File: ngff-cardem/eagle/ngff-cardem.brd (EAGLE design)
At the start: 90 x 100 mm, 150 parts, among them IC201 CB3Q3244PW, IC202 CB3Q3244PW, IC203 IP4234CZ6, IC204 FPF2109, IC205 FPF2109, IC301 TPS22958N-DGN, IC302 TPS22958N-DGK, J301 PJ-002BH-SMT-TR, M2 MENTOR_12701001, M3 MENTOR_12701001, Q201 12MHz, T101 BC850, T102 BC850, U201 IP4234CZ6, U202 AT91SAM3S-AU, U301 MIC5366-1.8YC5, X101 PINHD-2X3-SP, X102 ZX360D-B-10P(30), X201 MINI-USB-SHIELD-UX60-MB-5ST, X202 2.54mm, X203 JACK2.5_SJ-2523, X301 171826-4-RA

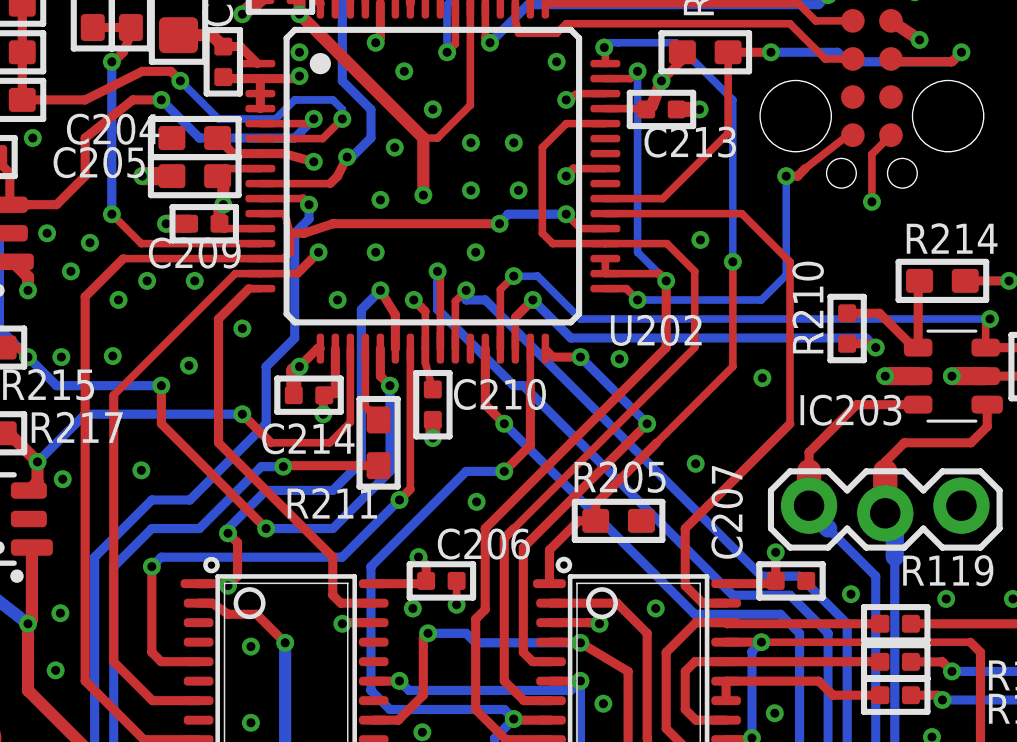
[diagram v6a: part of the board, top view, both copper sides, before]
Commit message: ngff-cardem: insert 2 PUs as DNP for possible !CONNECT_UART{1,2} biasing
solves SYS#5532
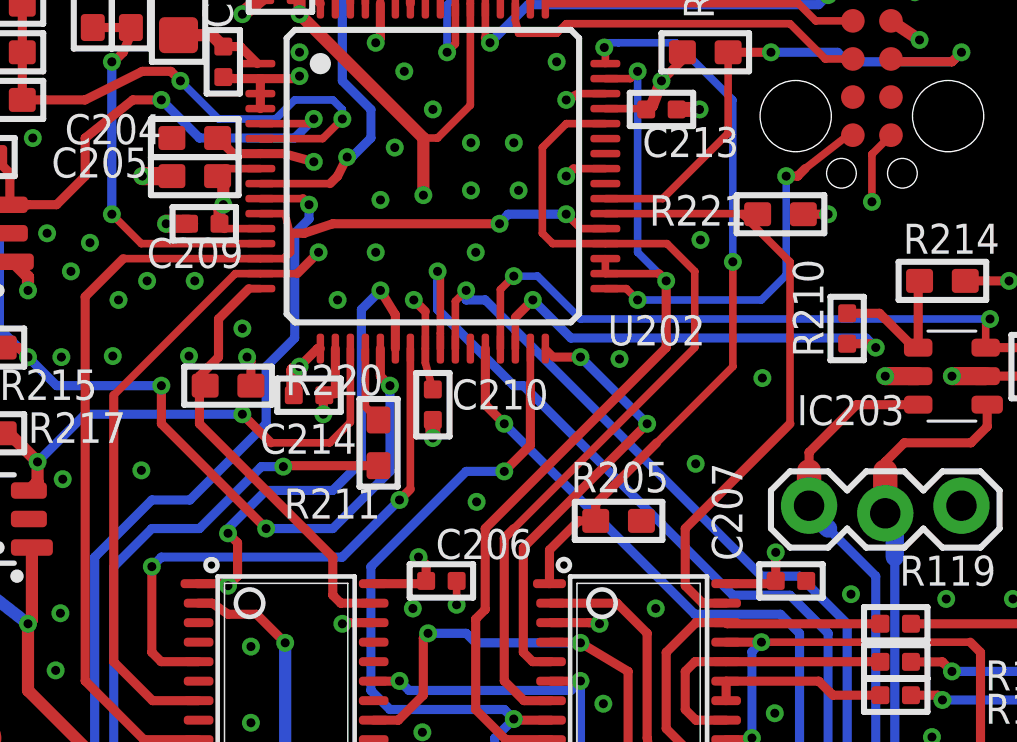
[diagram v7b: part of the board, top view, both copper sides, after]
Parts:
- added R220, R221: DNP, rc-sysmocom:_0603
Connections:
- net !CONNECT_UART1: now also R220.2
- net !CONNECT_UART2: now also R221.2
- net VCC_3V3: now also R220.1, R221.1
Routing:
- net VCC_3V3: track 56.6 -> 58.5 mm, vias 26 -> 28
- net !CONNECT_UART1: track 14.1 -> 14.8 mm
- net !CONNECT_UART2: track 20.7 -> 21.2 mm
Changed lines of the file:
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@@
 <attribute name="NAME" x="88.4875" y="77.31" size="1.1" layer="25" ratio="15" rot="R180"/>
 <attribute name="VALUE" x="89.3775" y="90.5825" size="1.27" layer="27" rot="R180"/>
-<attribute name="DESCRIPTION" value="" x="84.9325" y="83.5975" size="1.778" layer="27" rot="R180" display="off"/>
-<attribute name="MANUFACTURER" value="" x="84.9325" y="83.5975" size="1.778" layer="27" rot="R180" display="off"/>
-<attribute name="MANUFACTURERPARTNUMBER" value="" x="84.9325" y="83.5975" size="1.778" layer="27" rot="R180" display="off"/>
+<attribute name="DESCRIPTION" value="NO DESCRIPTION" x="84.9325" y="83.5975" size="1.778" layer="27" rot="R180" display="off"/>
+<attribute name="MANUFACTURER" value="UNKNOWN MANUFACTURER" x="84.9325" y="83.5975" size="1.778" layer="27" rot="R180" display="off"/>
+<attribute name="MANUFACTURERPARTNUMBER" value="UNKNOWN MANUFACTURER PART NUMBER" x="84.9325" y="83.5975" size="1.778" layer="27" rot="R180" display="off"/>
 <attribute name="SOURCE" value="DIGIKEY" x="84.9325" y="83.5975" size="1.778" layer="27" rot="R180" display="off"/>
-<attribute name="SOURCEPARTNUMBER" value="" x="84.9325" y="83.5975" size="1.778" layer="27" rot="R180" display="off"/>
-<attribute name="ROHSCERTIFICATE" value="" x="84.9325" y="83.5975" size="1.778" layer="27" rot="R180" display="off"/>
+<attribute name="SOURCEPARTNUMBER" value="UNKNOWN SOURCE PART NUMBER" x="84.9325" y="83.5975" size="1.778" layer="27" rot="R180" display="off"/>
+<attribute name="ROHSCERTIFICATE" value="UNKNOWN ROHS CERTIFICATE" x="84.9325" y="83.5975" size="1.778" layer="27" rot="R180" display="off"/>
 <attribute name="POPULATED" value="TRUE" x="84.9325" y="83.5975" size="1.778" layer="27" rot="R180" display="off"/>
 <attribute name="CLASS" value="CONNECTOR" x="84.9325" y="83.5975" size="1.778" layer="27" rot="R180" display="off"/>
@@
 <attribute name="ROHSCERTIFICATE" value="UNKNOWN ROHS CERTIFICATE" x="4.30375" y="20.495" size="1.016" layer="27" ratio="14" display="off"/>
 </element>
+<element name="R220" library="rc-sysmocom" package="_0603" value="DNP" x="13.0175" y="68.8975" smashed="yes" rot="R180">
+<attribute name="DESCRIPTION" value="NO DESCRIPTION" x="13.0175" y="68.8975" size="1.778" layer="27" rot="R180" display="off"/>
+<attribute name="MANUFACTURER" value="UNKNOWN MANUFACTURER" x="13.0175" y="68.8975" size="1.778" layer="27" rot="R180" display="off"/>
+<attribute name="MANUFACTURERPARTNUMBER" value="UNKNOWN MANUFACTURER PART NUMBER" x="13.0175" y="68.8975" size="1.778" layer="27" rot="R180" display="off"/>
+<attribute name="SOURCE" value="UNKNOWN SOURCE" x="13.0175" y="68.8975" size="1.778" layer="27" rot="R180" display="off"/>
+<attribute name="SOURCEPARTNUMBER" value="UNKNOWN SOURCE PART NUMBER" x="13.0175" y="68.8975" size="1.778" layer="27" rot="R180" display="off"/>
+<attribute name="ROHSCERTIFICATE" value="UNKNOWN ROHS CERTIFICATE" x="13.0175" y="68.8975" size="1.778" layer="27" rot="R180" display="off"/>
+<attribute name="POPULATED" value="FALSE" x="13.0175" y="68.8975" size="1.778" layer="27" rot="R180" display="off"/>
+<attribute name="CLASS" value="RESISTOR" x="13.0175" y="68.8975" size="1.778" layer="27" rot="R180" display="off"/>
+<attribute name="LINK" value="UNKNOWN LINK" x="13.0175" y="68.8975" size="1.778" layer="27" rot="R180" display="off"/>
+<attribute name="NAME" x="14.9225" y="68.58" size="1.016" layer="25" font="vector" ratio="14"/>
+<attribute name="VALUE" x="14.605" y="70.3898" size="0.508" layer="27" font="vector" ratio="10" rot="R180"/>
+</element>
+<element name="R221" library="rc-sysmocom" package="_0603" value="DNP" x="31.4325" y="74.6125" smashed="yes" rot="R180">
+<attribute name="DESCRIPTION" value="NO DESCRIPTION" x="31.4325" y="74.6125" size="1.778" layer="27" rot="R180" display="off"/>
+<attribute name="POPULATED" value="FALSE" x="31.4325" y="74.6125" size="1.778" layer="27" rot="R180" display="off"/>
+<attribute name="ROHSCERTIFICATE" value="UNKNOWN ROHS CERTIFICATE" x="31.4325" y="74.6125" size="1.778" layer="27" rot="R180" display="off"/>
+<attribute name="MANUFACTURER" value="UNKNOWN MANUFACTURER" x="31.4325" y="74.6125" size="1.778" layer="27" rot="R180" display="off"/>
+<attribute name="SOURCE" value="UNKNOWN SOURCE" x="31.4325" y="74.6125" size="1.778" layer="27" rot="R180" display="off"/>
+<attribute name="LINK" value="UNKNOWN LINK" x="31.4325" y="74.6125" size="1.778" layer="27" rot="R180" display="off"/>
+<attribute name="CLASS" value="RESISTOR" x="31.4325" y="74.6125" size="1.778" layer="27" rot="R180" display="off"/>
+<attribute name="MANUFACTURERPARTNUMBER" value="UNKNOWN MANUFACTURER PART NUMBER" x="31.4325" y="74.6125" size="1.778" layer="27" rot="R180" display="off"/>
+<attribute name="SOURCEPARTNUMBER" value="UNKNOWN SOURCE PART NUMBER" x="31.4325" y="74.6125" size="1.778" layer="27" rot="R180" display="off"/>
+<attribute name="NAME" x="30.32125" y="75.2475" size="1.016" layer="25" font="vector" ratio="14" rot="R180"/>
+<attribute name="VALUE" x="33.02" y="76.1048" size="0.508" layer="27" font="vector" ratio="10" rot="R180"/>
+</element>
 </elements>
 <signals>
@@
 <via x="11.08125" y="55.597" extent="1-16" drill="0.3"/>
 <via x="10.12875" y="66.0745" extent="1-16" drill="0.3"/>
-<via x="11.71625" y="69.567" extent="1-16" drill="0.3"/>
+<via x="11.71625" y="69.8845" extent="1-16" drill="0.3"/>
 <via x="9.17625" y="69.8845" extent="1-16" drill="0.3"/>
 <via x="8.415" y="73.66" extent="1-16" drill="0.3"/>
@@
 <wire x1="14.095" y1="72.1325" x2="13.7125" y2="72.1325" width="0.254" layer="1"/>
 <wire x1="13.7125" y1="72.1325" x2="12.7" y2="71.12" width="0.3048" layer="1"/>
-<wire x1="12.7" y1="71.12" x2="12.7" y2="66.9925" width="0.3048" layer="1"/>
-<wire x1="12.7" y1="66.9925" x2="16.51" y2="63.1825" width="0.3048" layer="1"/>
+<wire x1="12.7" y1="71.12" x2="12.7" y2="69.85" width="0.3048" layer="1"/>
+<wire x1="12.7" y1="69.85" x2="12.065" y2="69.215" width="0.3048" layer="1"/>
+<wire x1="12.065" y1="69.215" x2="12.065" y2="68.8975" width="0.3048" layer="1"/>
+<wire x1="12.065" y1="68.8975" x2="12.065" y2="67.6275" width="0.3048" layer="1"/>
+<wire x1="12.065" y1="67.6275" x2="16.51" y2="63.1825" width="0.3048" layer="1"/>
 <wire x1="16.51" y1="63.1825" x2="16.51" y2="61.9125" width="0.3048" layer="1"/>
 <wire x1="16.51" y1="61.9125" x2="16.775" y2="61.6475" width="0.3048" layer="1"/>
 <wire x1="17.8728" y1="61.6475" x2="16.775" y2="61.6475" width="0.3048" layer="1"/>
+<contactref element="R220" pad="2"/>
+<wire x1="12.2555" y1="68.8975" x2="12.065" y2="68.8975" width="0.3048" layer="1"/>
 </signal>
 <signal name="VERSION_DETECT">
@@
 <contactref element="IC302" pad="1"/>
 <contactref element="IC302" pad="4"/>
+<contactref element="R220" pad="1"/>
+<contactref element="R221" pad="1"/>
+<wire x1="32.1945" y1="74.6125" x2="33.02" y2="74.6125" width="0.3048" layer="1"/>
+<via x="33.02" y="74.6125" extent="1-16" drill="0.3"/>
+<wire x1="13.7795" y1="68.8975" x2="13.7795" y2="69.723" width="0.3048" layer="1"/>
+<wire x1="13.7795" y1="69.723" x2="13.6525" y2="69.85" width="0.3048" layer="1"/>
+<via x="13.6525" y="69.85" extent="1-16" drill="0.3"/>
 </signal>
 <signal name="ST_UART2_IO">
@@
 <wire x1="28.2575" y1="64.135" x2="31.75" y2="67.6275" width="0.3048" layer="1"/>
 <wire x1="31.75" y1="67.6275" x2="31.75" y2="73.025" width="0.254" layer="1"/>
-<wire x1="31.75" y1="73.025" x2="30.1425" y2="74.6325" width="0.254" layer="1"/>
+<wire x1="31.75" y1="73.025" x2="30.1625" y2="74.6125" width="0.254" layer="1"/>
+<wire x1="30.1625" y1="74.6125" x2="30.1425" y2="74.6325" width="0.254" layer="1"/>
 <wire x1="30.1425" y1="74.6325" x2="25.595" y2="74.6325" width="0.254" layer="1"/>
+<contactref element="R221" pad="2"/>
+<wire x1="30.6705" y1="74.6125" x2="30.1625" y2="74.6125" width="0.3048" layer="1"/>
 </signal>
 <signal name="N$1">

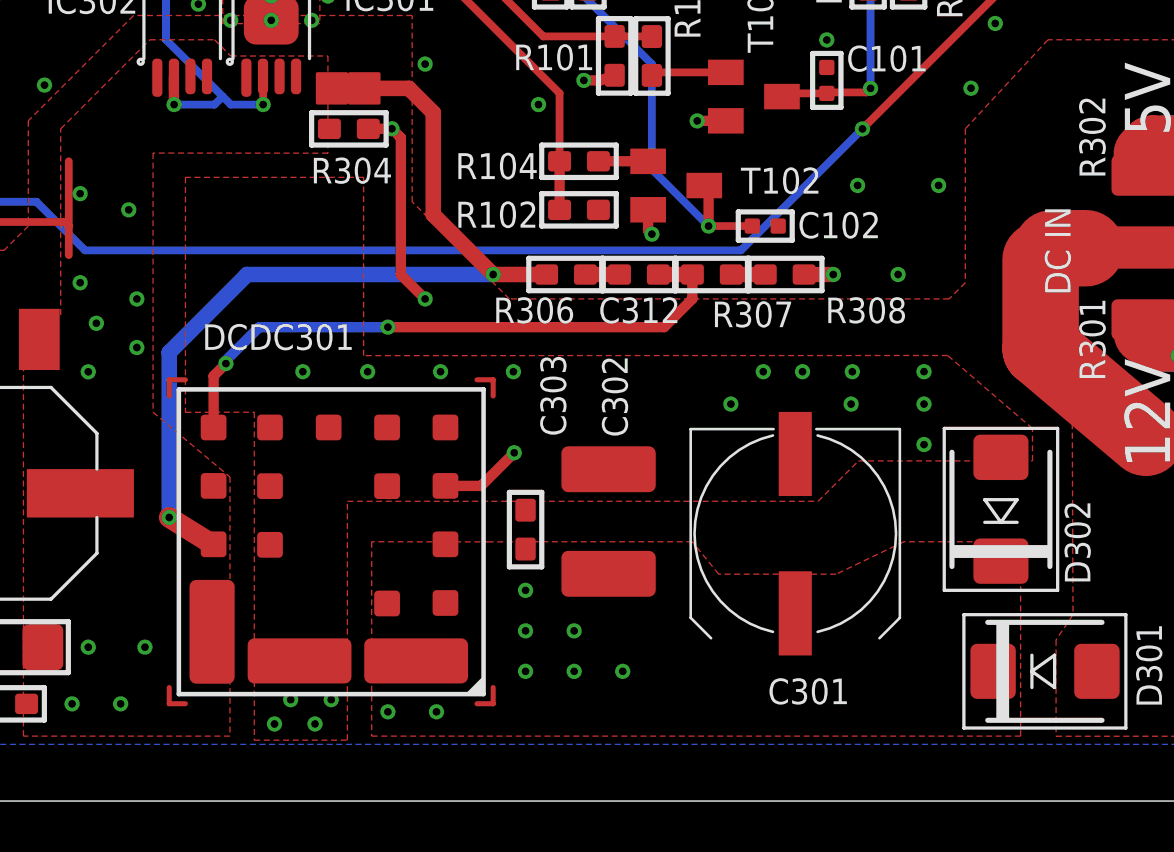
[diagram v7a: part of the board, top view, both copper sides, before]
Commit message: ngff-cardem: add PU+PD footpint for DCDC ENA input (solves SYS#5519)
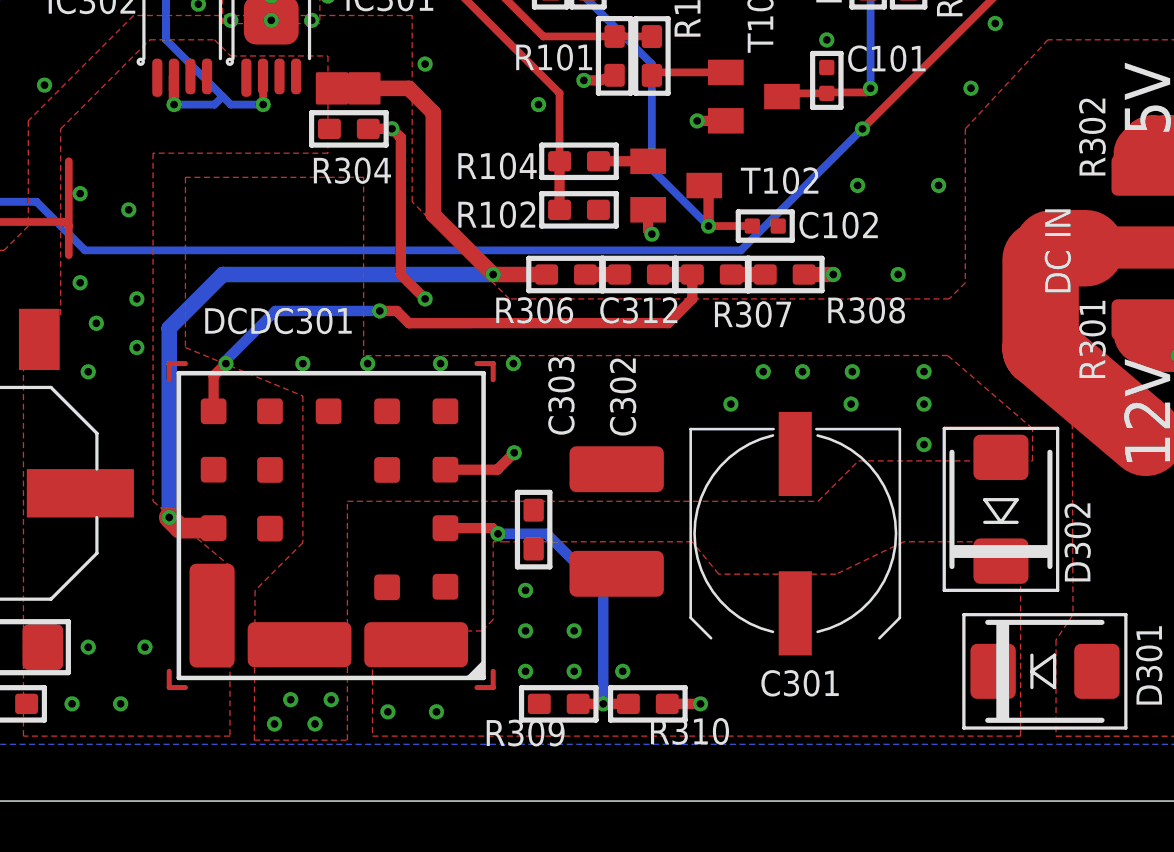
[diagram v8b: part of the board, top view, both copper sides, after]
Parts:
- added R309, R310: DNP, rc-sysmocom:_0603
- moved DCDC301 0.64 mm to (40.1, 10.8)
- moved C302 0.32 mm to (51.3, 11.0)
- moved C303 0.32 mm to (48.1, 10.6)
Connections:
- new net N$25: DCDC301.1, R309.2, R310.1
- net +VIN_PROT: now also R309.1; no longer DCDC301.1
- net GND: now also R310.2
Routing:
- net N$25: track 0.00 -> 13.6 mm, vias 0 -> 2
- net GND: track 102.9 -> 104.2 mm, vias 332 -> 333
- net N$13: track 19.1 -> 18.6 mm
